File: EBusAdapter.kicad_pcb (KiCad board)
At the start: 2 copper layers, 100 x 50 mm, 31 parts, among them CON1 BARREL_JACK, P1 CONN_01X02, P2 CONN_01X06, P3 CONN_01X04, P4 CONN_01X04, Q1 BC547, U1 4011, U2 LM78L05ACZ, U3 ADuM1201AR, U4 PHOTON, U5 LM7805CT

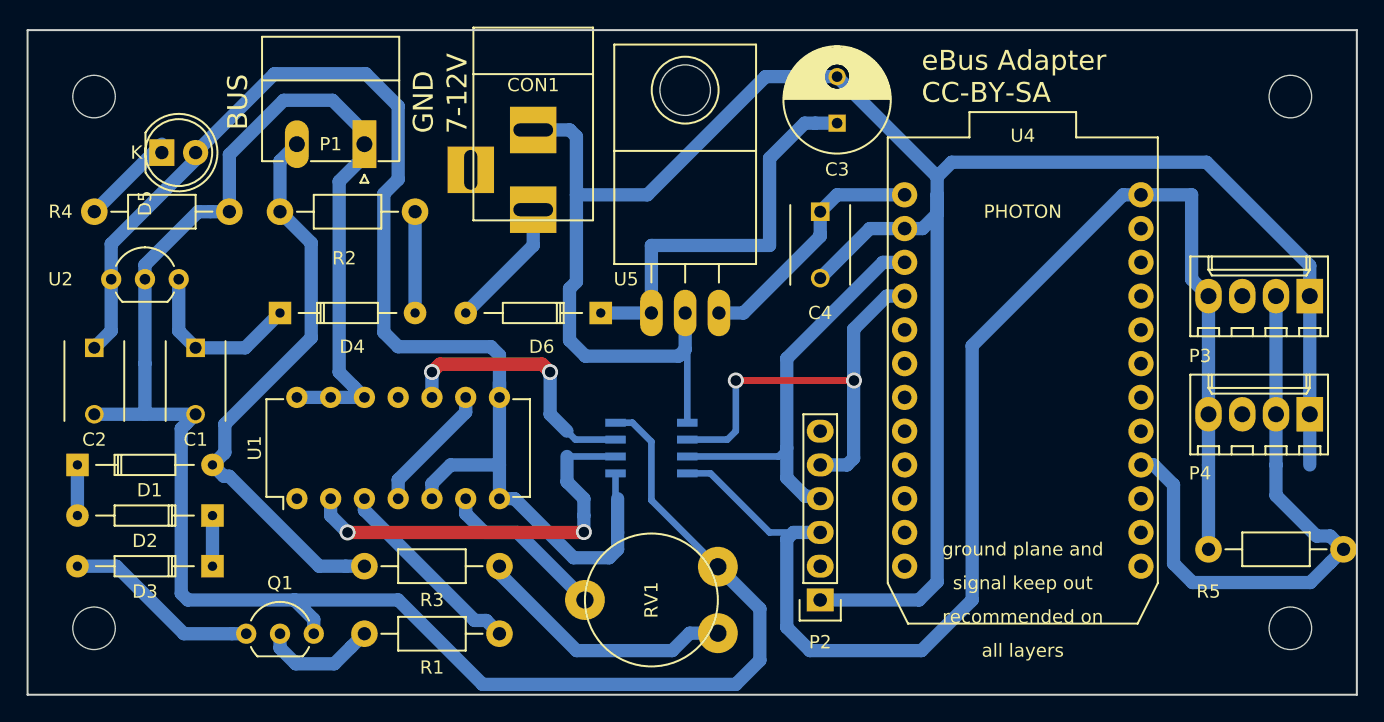
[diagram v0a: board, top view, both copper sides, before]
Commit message: Fix CD4011 power supply (was inverted) - added logo
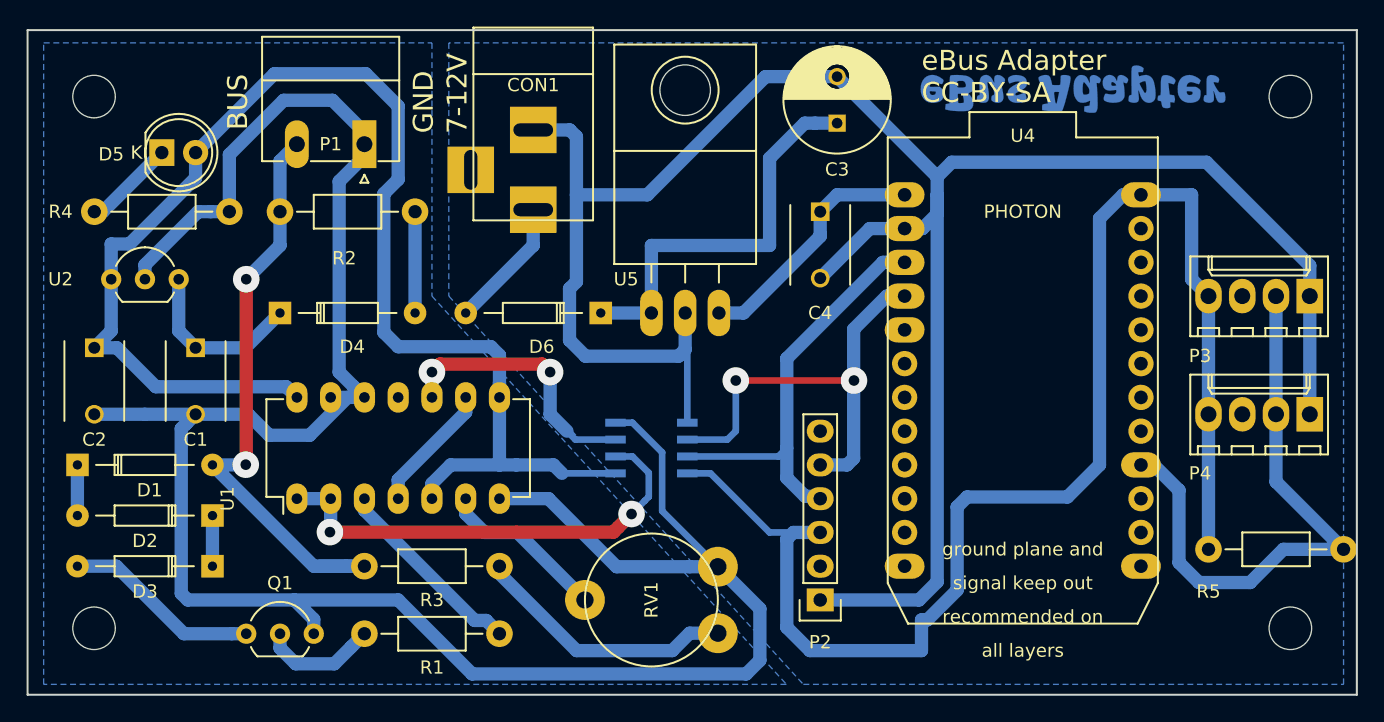
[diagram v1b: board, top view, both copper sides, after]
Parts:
- added G***: LOGO, ebus-adapter:logo-ebus-adapter, B.Cu at (233.7, 64.8)
- U1: footprint Housings_DIP:DIP-14_W7.62mm -> Housings_DIP:DIP-14_W7.62mm_LongPads
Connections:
- U1 pad 14: GND -> VCC
- U1 pad 7: VCC -> GND
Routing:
- net GND: track 157.9 -> 176.4 mm
- net VCC: track 98.4 -> 106.2 mm
- net +3V3: track 105.0 -> 109.7 mm
- net Net-(U1-Pad1): track 30.7 -> 35.0 mm
- net GNDD: track 169.4 -> 165.6 mm
- net Net-(D1-Pad2): track 43.3 -> 46.2 mm, vias 0 -> 2
- net Net-(P3-Pad2): track 45.2 -> 44.3 mm
- added copper zone on B.Cu, net GND
- added copper zone on B.Cu, net GNDD
